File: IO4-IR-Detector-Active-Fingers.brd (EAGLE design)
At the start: 103 x 107.4 mm, 48 parts, among them J1 0.100, J10 0.100, J11 0.100, J12 0.100, J13 0.100, J14 0.100, J15 0.100, J16 0.100, J2 0.100, J3 0.100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

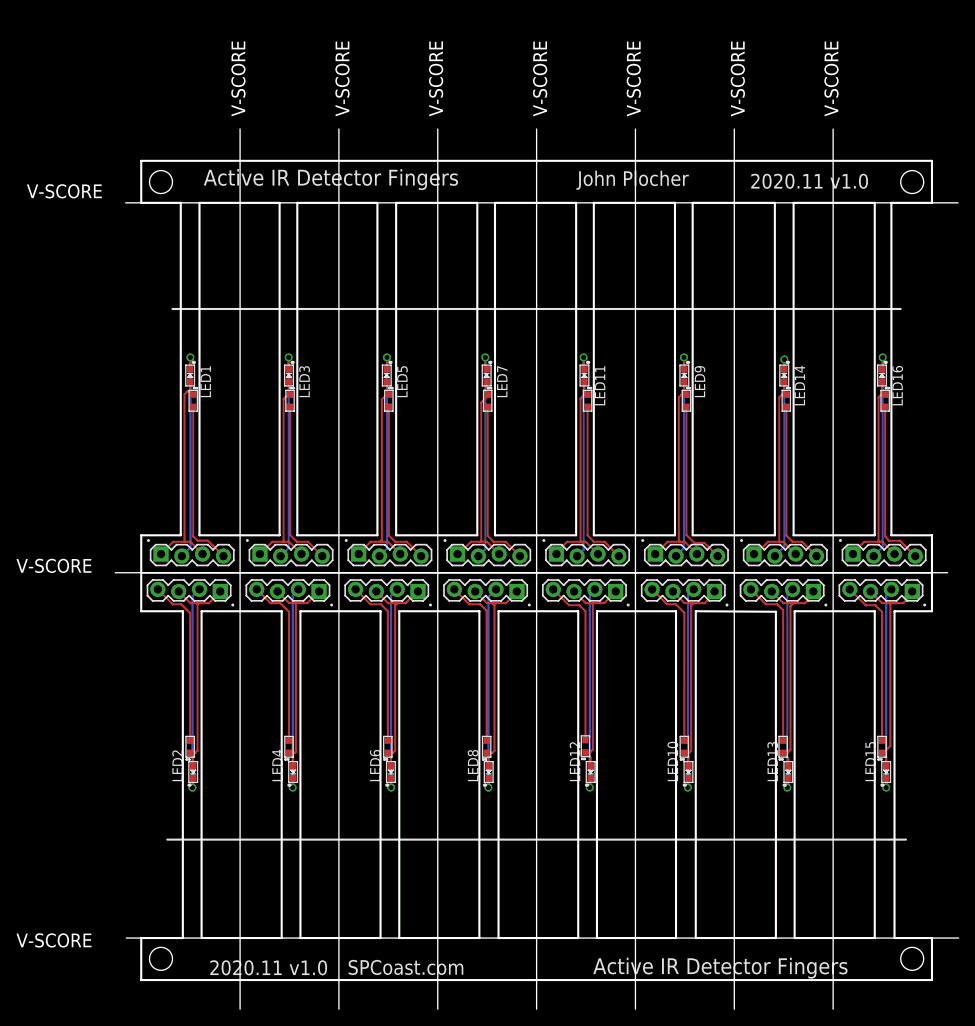
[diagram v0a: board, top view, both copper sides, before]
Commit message: JLC requires 6mm board width, switch to QRE1113GR
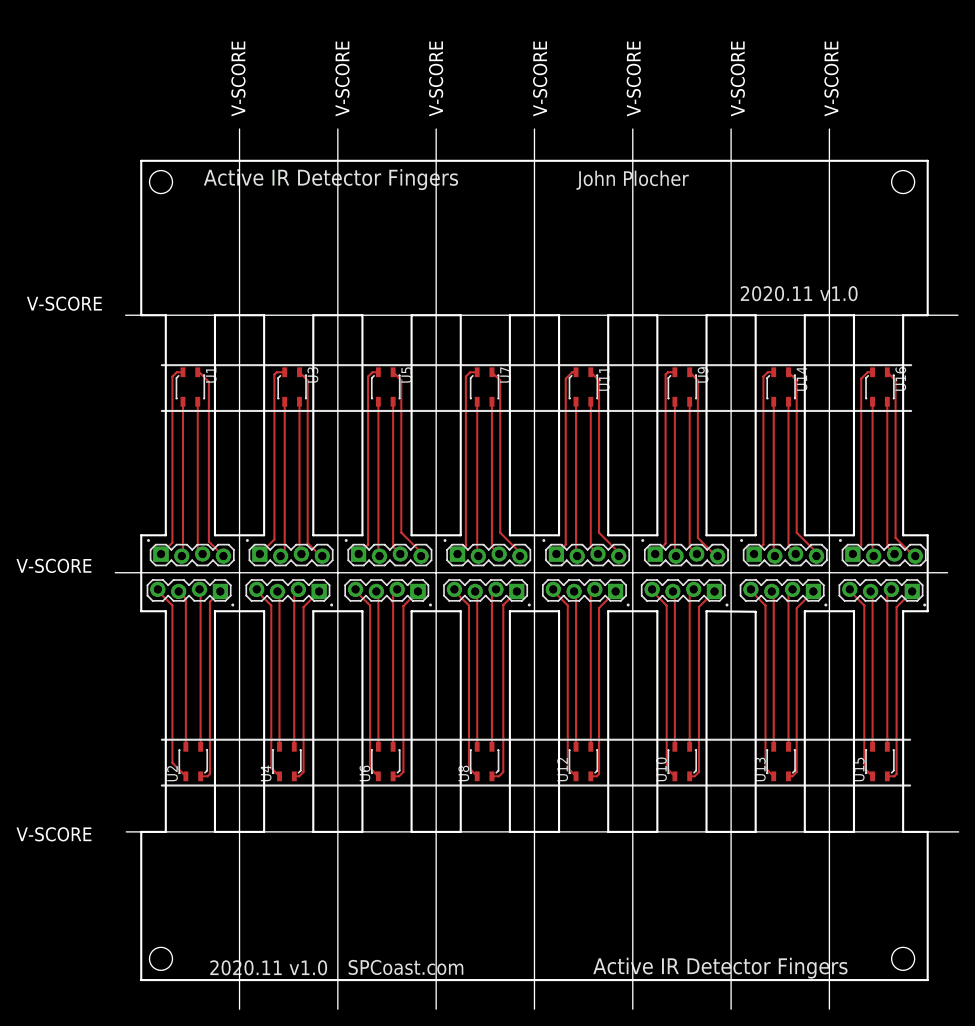
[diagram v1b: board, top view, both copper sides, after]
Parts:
- removed LED1, LED10, LED11, LED12, LED13, LED14, LED15, LED16, LED2, LED3, LED4, LED5, LED6, LED7, LED8, LED9: (no value), SPCoast:0603-LED
- removed T.DETECTED1, T.DETECTED10, T.DETECTED11, T.DETECTED12, T.DETECTED13, T.DETECTED14, T.DETECTED15, T.DETECTED16, T.DETECTED2, T.DETECTED3, T.DETECTED4, T.DETECTED5, T.DETECTED6, T.DETECTED7, T.DETECTED8, T.DETECTED9: PT19-21C/L41, SPCoast:ALS-PT19
- added U1, U10, U11, U12, U13, U14, U15, U16, U2, U3, U4, U5, U6, U7, U8, U9: QRE1113, SPCoast:QRE1113
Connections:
- new net N$12: J10.1, U10.1
- new net N$16: J14.1, U14.1
- new net N$20: J2.2, U2.2
- new net N$24: J3.1, U3.1
- new net N$28: J5.1, U5.1
- new net N$32: J7.4, U7.4
- new net N$4: J4.4, U4.4
- new net N$57: J14.2, U14.2
- new net N$58: J15.4, U15.4
- new net N$59: J15.2, U15.2
- new net N$60: J16.4, U16.4
- new net N$61: J16.2, U16.2
- new net N$62: J10.3, U10.3
- new net N$63: J9.3, U9.3
- new net N$64: J6.3, U6.3
- new net N$8: J6.1, U6.1
- net N$1: now also U1.4; no longer T.DETECTED1.E
- net N$10: now also J8.1, U8.1; no longer J3.1, J3.3, LED3.A, T.DETECTED3.C
- net N$11: now also J9.1, U9.1; no longer J3.2, LED3.C
- net N$13: now also J11.1, U11.1; no longer J4.4, T.DETECTED4.E
- net N$14: now also J12.1, U12.1; no longer J4.1, J4.3, LED4.A, T.DETECTED4.C
- net N$15: now also J13.1, U13.1; no longer J4.2, LED4.C
- net N$17: now also J15.1, U15.1; no longer J5.4, T.DETECTED5.E
- net N$18: now also J16.1, U16.1; no longer J5.1, J5.3, LED5.A, T.DETECTED5.C
- net N$19: now also J2.4, U2.4; no longer J5.2, LED5.C
- net N$2: now also U1.2; no longer LED1.C
- net N$21: now also J2.1, U2.1; no longer J6.4, T.DETECTED6.E
- net N$22: now also J3.4, U3.4; no longer J6.1, J6.3, LED6.A, T.DETECTED6.C
- net N$23: now also J3.2, U3.2; no longer J6.2, LED6.C
- net N$25: now also J2.3, U2.3; no longer J8.4, T.DETECTED7.E
- net N$26: now also J5.4, U5.4; no longer J8.2, LED8.C
- net N$27: now also J5.2, U5.2; no longer J8.1, J8.3, LED8.A, T.DETECTED7.C
- net N$29: now also J6.4, U6.4; no longer J7.4, T.DETECTED8.E
- net N$3: now also U1.1; no longer J1.3, LED1.A, T.DETECTED1.C
- net N$30: now also J6.2, U6.2; no longer J7.2, LED7.C
- net N$31: now also J3.3, U3.3; no longer J7.1, J7.3, LED7.A, T.DETECTED8.C
- net N$33: now also J7.2, U7.2; no longer J9.4, T.DETECTED9.E
- net N$34: now also J4.3, U4.3; no longer J9.1, J9.3, LED9.A, T.DETECTED9.C
- net N$35: now also J8.4, U8.4; no longer J10.4, T.DETECTED10.E
- net N$36: now also J8.2, U8.2; no longer J10.1, J10.3, LED10.A, T.DETECTED10.C
- net N$37: now also J5.3, U5.3; no longer J11.4, T.DETECTED11.E
- net N$38: now also J9.4, U9.4; no longer J11.1, J11.3, LED11.A, T.DETECTED11.C
- net N$39: now also J9.2, U9.2; no longer J12.4, T.DETECTED12.E
- net N$40: now also J7.3, U7.3; no longer J12.1, J12.3, LED12.A, T.DETECTED12.C
- net N$41: now also J8.3, U8.3; no longer J13.4, T.DETECTED13.E
- net N$42: now also J16.3, U16.3; no longer J13.1, J13.3, LED13.A, T.DETECTED13.C
- net N$43: now also J15.3, U15.3; no longer J14.4, T.DETECTED14.E
- net N$44: now also U14.3; no longer J14.1, LED14.A, T.DETECTED14.C
- net N$45: now also J10.4, U10.4; no longer J15.4, T.DETECTED15.E
- net N$46: now also J10.2, U10.2; no longer J15.1, J15.3, LED15.A, T.DETECTED15.C
- net N$47: now also J13.3, U13.3; no longer J16.4, T.DETECTED16.E
- net N$48: now also J11.4, U11.4; no longer J16.1, J16.3, LED16.A, T.DETECTED16.C
- net N$49: now also J11.2, U11.2; no longer J9.2, LED9.C
- net N$5: now also J4.2, U4.2; no longer J2.4, T.DETECTED2.E
- net N$50: now also J12.3, U12.3; no longer J10.2, LED10.C
- net N$51: now also J12.4, U12.4; no longer J11.2, LED11.C
- net N$52: now also U12.2; no longer LED12.C
- net N$53: now also J13.4, U13.4; no longer J13.2, LED13.C
- net N$54: now also J13.2, U13.2; no longer J14.2, LED14.C
- net N$55: now also J11.3, U11.3; no longer J15.2, LED15.C
- net N$56: now also J14.4, U14.4; no longer J16.2, LED16.C
- net N$6: now also J4.1, U4.1; no longer J2.1, J2.3, LED2.A, T.DETECTED2.C
- net N$7: now also J1.3, U1.3; no longer J2.2, LED2.C
- net N$9: now also J7.1, U7.1; no longer J3.4, T.DETECTED3.E
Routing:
- net N$8: track 0.00 -> 24.2 mm
- net N$12: track 0.00 -> 24.2 mm
- net N$24: track 0.00 -> 24.0 mm
- net N$58: track 0.00 -> 24.0 mm
- net N$4: track 0.00 -> 24.0 mm
- net N$60: track 0.00 -> 24.0 mm
- net N$32: track 0.00 -> 23.9 mm
- net N$28: track 0.00 -> 23.6 mm
- net N$16: track 0.00 -> 23.6 mm
- net N$59: track 0.00 -> 19.4 mm
- net N$20: track 0.00 -> 19.3 mm
- net N$64: track 0.00 -> 19.1 mm
- net N$62: track 0.00 -> 19.1 mm
- net N$63: track 0.00 -> 18.9 mm
- net N$61: track 0.00 -> 18.9 mm
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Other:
- outline, holes or cut-outs redrawn
- board text added: "8' N-Scale"
- board text removed: "10' N-Scale"
